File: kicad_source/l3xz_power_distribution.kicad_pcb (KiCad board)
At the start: 2 copper layers, 124 x 30 mm, 34 parts, among them J1 PowerPole_ver, J10 PowerPole_ver, J11 PowerPole_ver, J12 PowerPole_ver, J2 PowerPole_ver, J3 PowerPole_ver, J4 PowerPole_ver, J5 PowerPole_ver, J6 PowerPole_ver, J7 PowerPole_ver, J8 PowerPole_ver, J9 PowerPole_ver

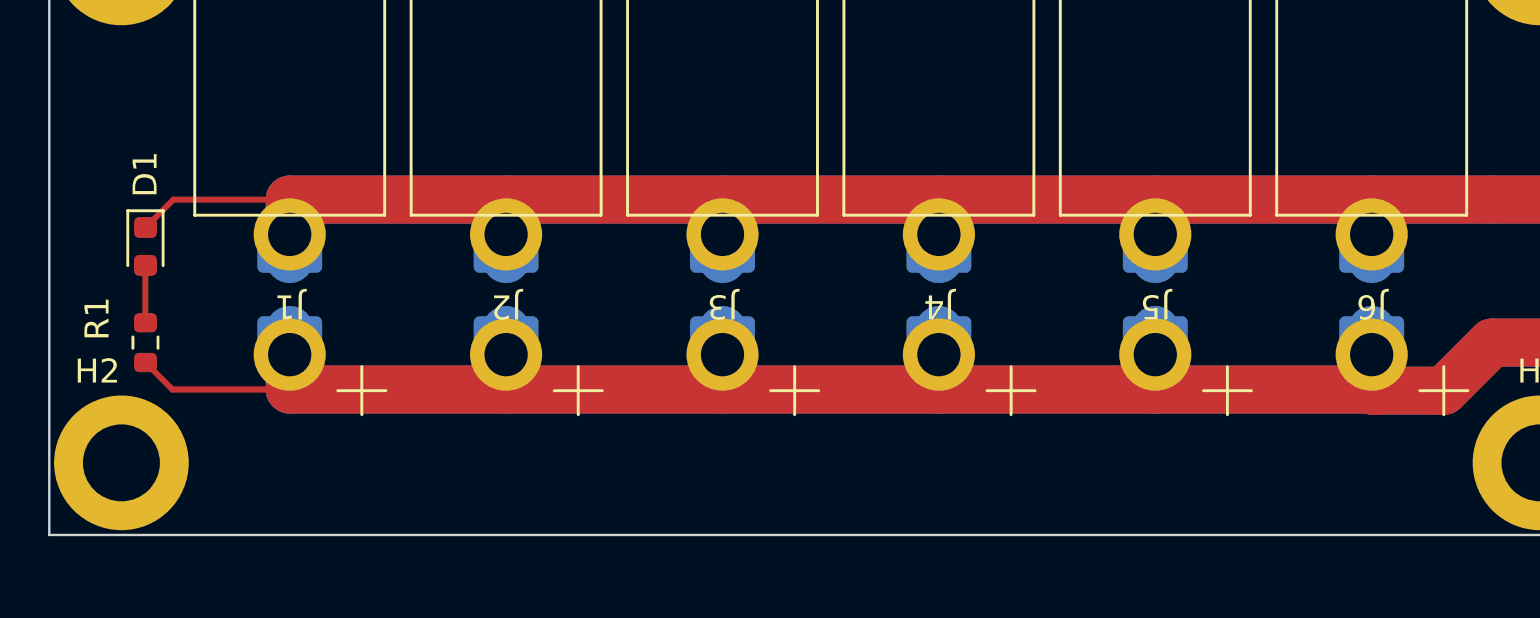
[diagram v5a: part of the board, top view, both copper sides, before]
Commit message: switched to THT for LED and resistor
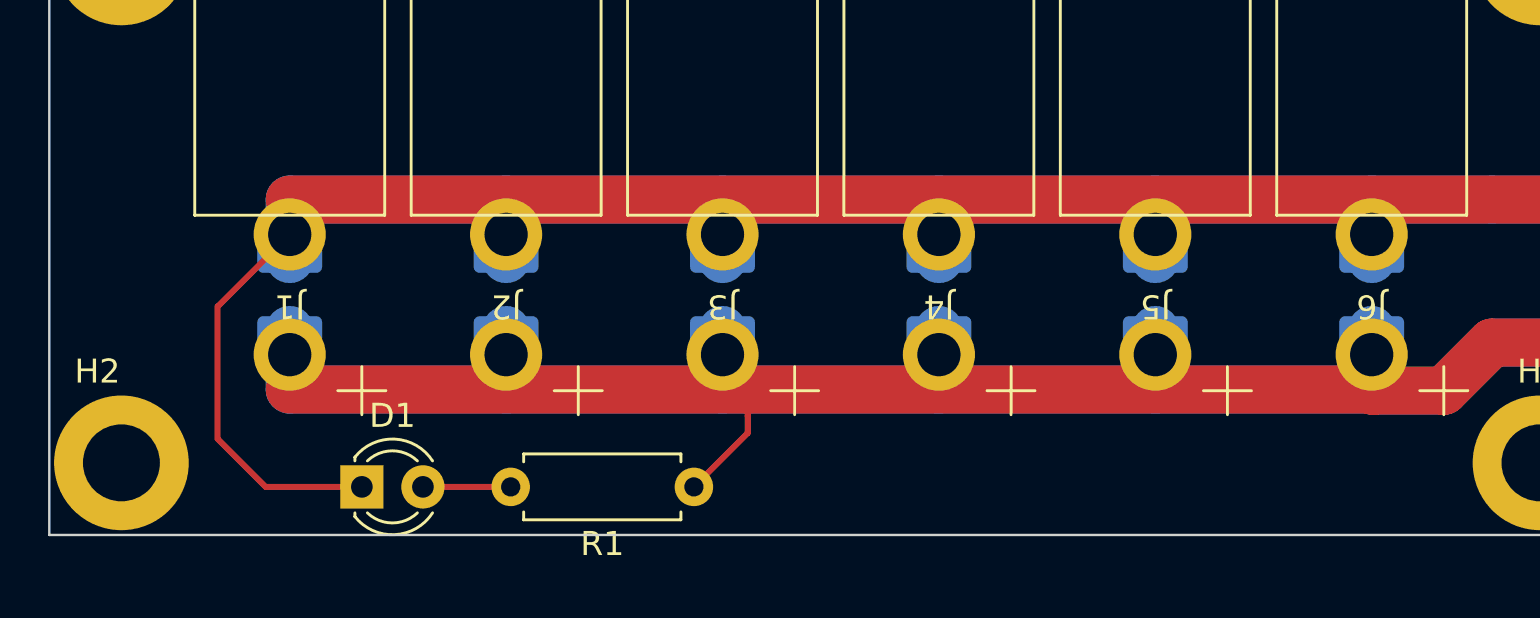
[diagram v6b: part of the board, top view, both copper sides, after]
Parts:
- D1: footprint LED_SMD:LED_0603_1608Metric -> LED_THT:LED_D3.0mm
- R1: footprint Resistor_SMD:R_0603_1608Metric -> Resistor_THT:R_Axial_DIN0207_L6.3mm_D2.5mm_P7.62mm_Horizontal
- moved R1 23.6 mm to (116.8, 108.0), turned to 180 degrees
- moved D1 13.5 mm to (103.0, 108.0), turned to 0 degrees
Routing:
- net GND: track 244.2 -> 254.3 mm
- net +BATT: track 247.5 -> 246.0 mm
- net Net-(D1-Pad2): track 2.39 -> 3.65 mm

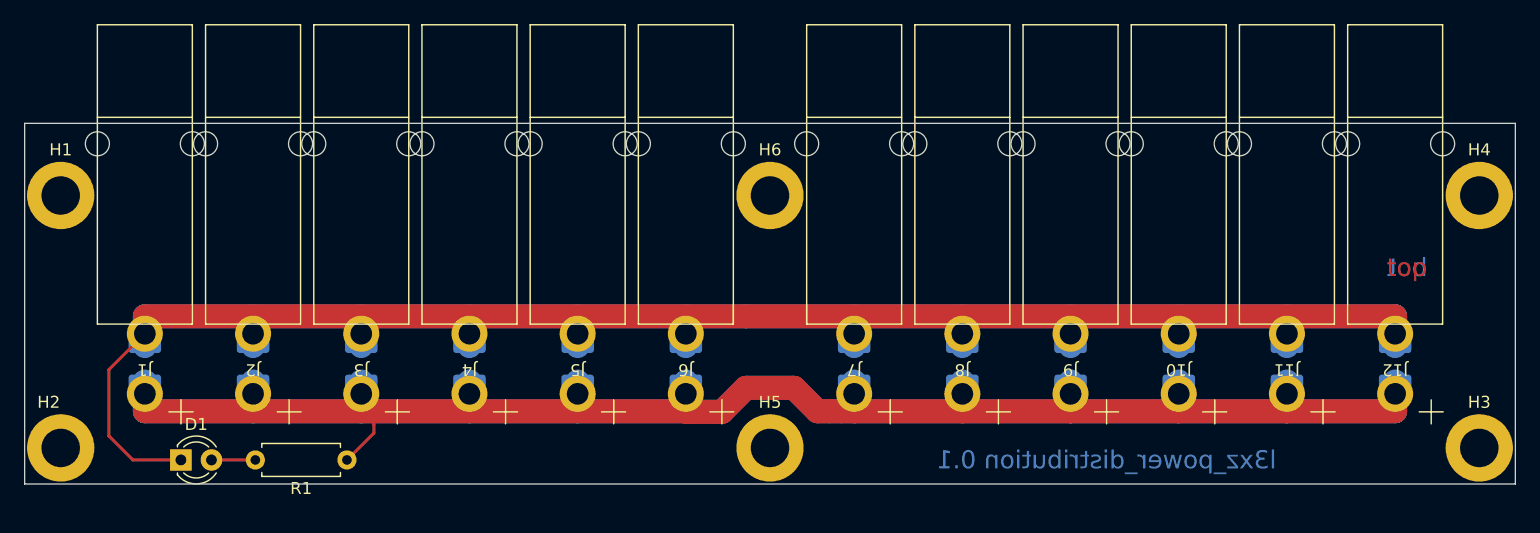
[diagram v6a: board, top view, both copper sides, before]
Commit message: added alternative footprint for power pole
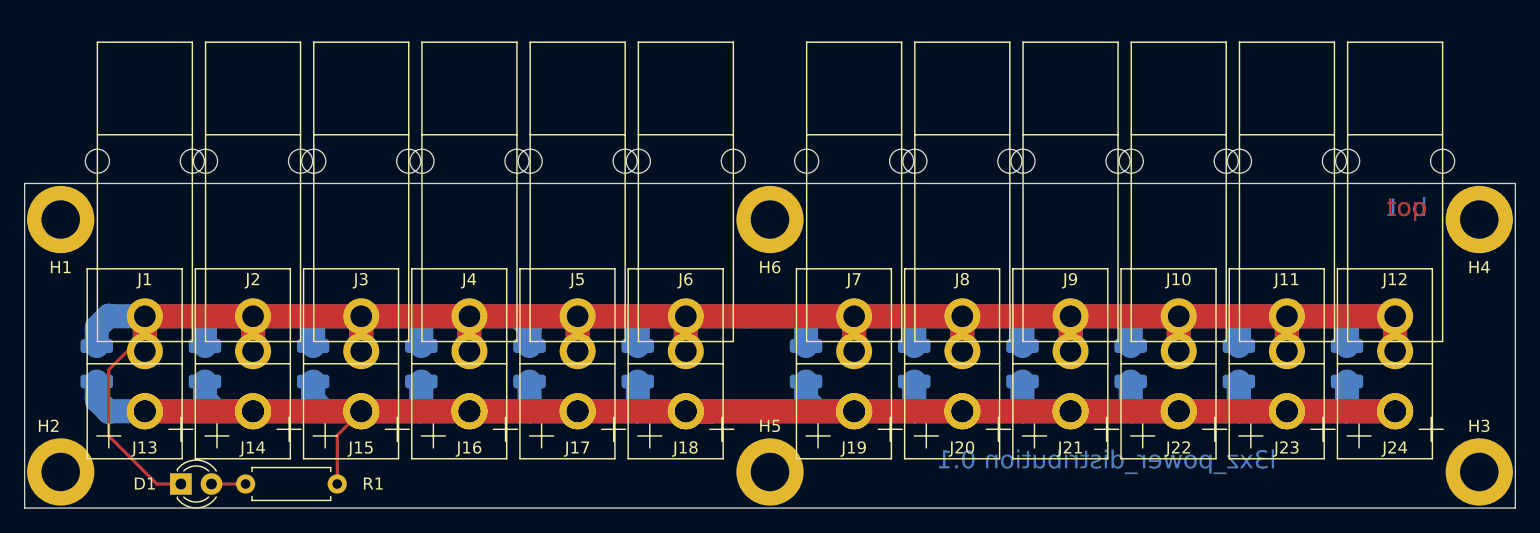
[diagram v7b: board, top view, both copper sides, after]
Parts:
- added J13: PowerPole_ver, generationmake:POWERPOLE_2, F.Cu at (100.0, 100.0)
- added J14: PowerPole_ver, generationmake:POWERPOLE_2, F.Cu at (109.0, 100.0)
- added J15: PowerPole_ver, generationmake:POWERPOLE_2, F.Cu at (118.0, 100.0)
- added J16: PowerPole_ver, generationmake:POWERPOLE_2, F.Cu at (127.0, 100.0)
- added J17: PowerPole_ver, generationmake:POWERPOLE_2, F.Cu at (136.0, 100.0)
- added J18: PowerPole_ver, generationmake:POWERPOLE_2, F.Cu at (145.0, 100.0)
- added J19: PowerPole_ver, generationmake:POWERPOLE_2, F.Cu at (159.0, 100.0)
- added J20: PowerPole_ver, generationmake:POWERPOLE_2, F.Cu at (168.0, 100.0)
- added J21: PowerPole_ver, generationmake:POWERPOLE_2, F.Cu at (177.0, 100.0)
- added J22: PowerPole_ver, generationmake:POWERPOLE_2, F.Cu at (186.0, 100.0)
- added J23: PowerPole_ver, generationmake:POWERPOLE_2, F.Cu at (195.0, 100.0)
- added J24: PowerPole_ver, generationmake:POWERPOLE_2, F.Cu at (204.0, 100.0)
- moved L1 19.4 mm to (134.0, 93.4)
- moved C1 4.00 mm to (96.0, 100.0)
- moved C10 4.00 mm to (182.0, 100.0)
- moved C11 4.00 mm to (191.0, 100.0)
- moved C12 4.00 mm to (200.0, 100.0)
- moved C2 4.00 mm to (105.0, 100.0)
- moved C3 4.00 mm to (114.0, 100.0)
- moved C4 4.00 mm to (123.0, 100.0)
- moved C5 4.00 mm to (132.0, 100.0)
- moved C6 4.00 mm to (141.0, 100.0)
- moved C7 4.00 mm to (155.0, 100.0)
- moved C8 4.00 mm to (164.0, 100.0)
- moved C9 4.00 mm to (173.0, 100.0)
- moved L2 3.16 mm to (104.0, 90.0)
- moved R1 2.16 mm to (116.0, 110.0)
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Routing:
- net GND: track 254.3 -> 323.7 mm
- net +BATT: track 246.0 -> 249.5 mm
- net Net-(D1-Pad2): track 3.65 -> 2.84 mm
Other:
- board size 124 x 30 mm -> 124 x 27 mm
